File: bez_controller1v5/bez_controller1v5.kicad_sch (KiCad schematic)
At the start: 87 parts, among them J1 Conn_01x03_Male, J10 Conn_01x07_Socket, J11 Conn_01x03_Male, J12 Conn_01x03_Male, J13 USB_B_Mini, J14 JTAG Conn_01x06_Male, J16 MOLEX_Conn_Button, J17 MOLEX_Conn_Button, J2 Conn_01x03_Male, J3 Conn_01x03_Male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

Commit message: First iteration of the new board with new functions
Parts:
- removed J14: JTAG Conn_01x06_Male, Connector_PinHeader_2.54mm:PinHeader_1x06_P2.54mm_Vertical, symbol Connector:Conn_01x06_Male
- added J14: PPTC041LGBN-RC, KiCad:CONN_PPTC041LGBN-RC_SUL, symbol 2024-11-01_01-45-54:PPTC041LGBN-RC
- added J15: Conn_01x03_Male, Connector_PinHeader_2.54mm:PinHeader_1x03_P2.54mm_Vertical, symbol Connector:Conn_01x03_Male
- C10: footprint Capacitor_THT:CP_Radial_D5.0mm_P2.00mm -> Capacitor_SMD:C_0603_1608Metric
- J11, J12, J2, J3, J6, J7: footprint Connector_Molex:Molex_SPOX_5267-03A_1x03_P2.50mm_Vertical -> KiCad:CONN_S3B-XH-ALFSN_JST
- J13: footprint USB-Library:USB_MINI -> KiCad:USB_MINI
- J16, J17: footprint 530480210:MOLEX_530480210 -> KiCad:CON_530480210_MOL
- R17, R9: footprint (none) -> Resistor_SMD:R_0603_1608Metric
- U11, U12, U2, U3, U8, U9: footprint Package_SO:VSSOP-8_3.0x3.0mm_P0.65mm -> KiCad:VSSOP-8_3.0x3.0mm_P0.65mm
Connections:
- net +12V: no longer C11.2, C12.2, C21.2, C22.2, C24.2, C25.2, J11.2 (Pin_2), J12.2 (Pin_2), J2.2 (Pin_2), J3.2 (Pin_2), J6.2 (Pin_2), J7.2 (Pin_2)
- net +3.3V: now also J14.2
- net GND: now also J14.1
- net INT1: now also U7.8 (PC0); no longer U7.51 (PC10)
- net INT2: now also U7.9 (PC1); no longer U7.52 (PC11)
- net SWO: now also J15.1 (Pin_1); no longer U7.55 (PB3)
- net USART3_TX: now also U7.51 (PC10); no longer U7.29 (PB10)
- net post_shunt_12v: now reaches C2.1, R3.2, U1.1 (VI), U6.4 (-)
- net post_shunt_12v: now also C11.2, C12.2, C21.2, C22.2, C24.2, C25.2, J11.2 (Pin_2), J12.2 (Pin_2), J2.2 (Pin_2), J3.2 (Pin_2), J6.2 (Pin_2), J7.2 (Pin_2)
- net GPIO3: no longer names the net of U7.2 (PC13)
- new net SWO_or_Screen_SDA: J15.2 (Pin_2), U7.55 (PB3)
- new net Screen_SCL: J14.3, U7.29 (PB10)
- new net Screen_SDA: J14.4, J15.3 (Pin_3)
- no-connect marks 26 -> 24
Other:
- note added: "Adding Screen I2C Connection"
- note added: "Configure SWO or Screen"

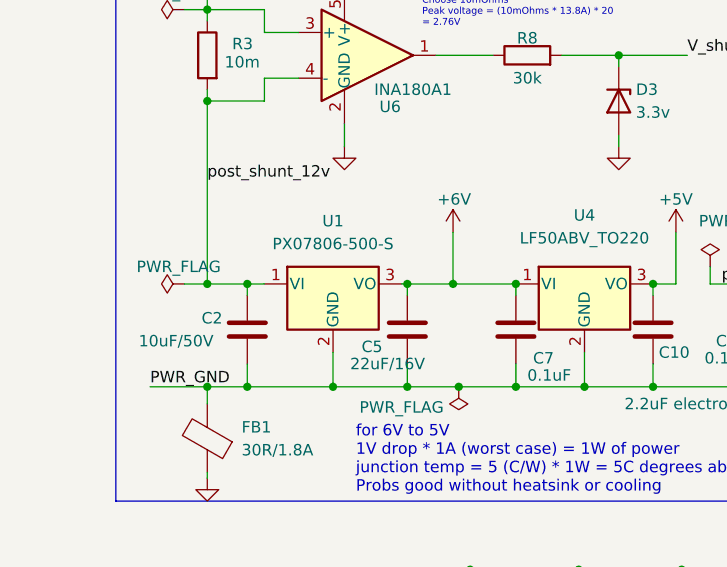
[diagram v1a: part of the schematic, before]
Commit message: -added label on each motor connections, -thickened 3.3v wires, removed uart line squiggles, updated U1 12v to 6v dcdc converter to new pxo7806-500
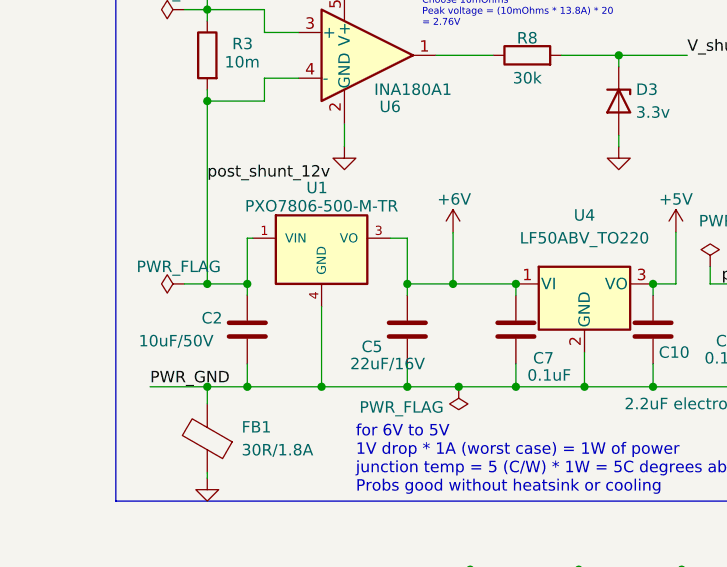
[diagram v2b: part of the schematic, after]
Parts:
- removed U1: PX07806-500-S, Package_TO_SOT_THT:TO-220F-3_Vertical, symbol Regulator_Linear:LM7805_TO220
- added U1: ~, KiCad:CONV_PXO7806-500-M-TR, symbol Regulator_Linear:PXO7806-500-M-TR
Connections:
- net +6V: now also U1.3 (VO)
- net PWR_GND: now also U1.4 (GND)
- net post_shunt_12v: now also U1.1 (VIN)
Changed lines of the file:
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@@
 	)
 	(junction
-		(at 36.83 68.58)
-		(diameter 0)
-		(color 0 0 0 0)
-	)
-	(junction
 		(at 43.18 182.88)
 		(diameter 0)
@@
 	)
 	(junction
+		(at 35.56 68.58)
+		(diameter 0)
+		(color 0 0 0 0)
+	)
+	(junction
 		(at 69.85 -52.07)
 		(diameter 0)
@@
 	(wire
 		(pts
+			(xy 35.56 68.58) (xy 45.085 68.58)
+		)
+		(stroke
+			(width 0)
+			(type default)
+		)
+	)
+	(wire
+		(pts
 			(xy 234.95 -102.235) (xy 267.97 -102.235)
 		)
@@
 	(wire
 		(pts
+			(xy 27.305 52.07) (xy 27.305 57.15)
+		)
+		(stroke
+			(width 0)
+			(type default)
+		)
+	)
+	(wire
+		(pts
 			(xy 121.92 96.52) (xy 121.92 99.06)
 		)
@@
 	(wire
 		(pts
-			(xy 27.305 57.15) (xy 29.21 57.15)
+			(xy 27.305 52.07) (xy 27.94 52.07)
 		)
 		(stroke
@@
 	(wire
 		(pts
-			(xy 44.45 57.15) (xy 45.085 57.15)
+			(xy 43.18 52.07) (xy 45.085 52.07)
 		)
 		(stroke
@@
 	(wire
 		(pts
+			(xy 45.085 52.07) (xy 45.085 57.15)
+		)
+		(stroke
+			(width 0)
+			(type default)
+		)
+	)
+	(wire
+		(pts
 			(xy 274.32 -102.235) (xy 274.32 -101.6)
 		)
@@
 	(wire
 		(pts
-			(xy 36.83 64.77) (xy 36.83 68.58)
+			(xy 35.56 59.69) (xy 35.56 68.58)
 		)
 		(stroke
@@
 	(wire
 		(pts
-			(xy 27.305 68.58) (xy 36.83 68.58)
+			(xy 27.305 68.58) (xy 35.56 68.58)
 		)
 		(stroke
@@
 	(wire
 		(pts
-			(xy 36.83 68.58) (xy 45.085 68.58)
-		)
-		(stroke
-			(width 0)
-			(type default)
-		)
-	)
-	(wire
-		(pts
 			(xy 138.43 53.34) (xy 145.415 53.34)
 		)
@@
 	)
 	(symbol
-		(lib_id "Regulator_Linear:LM7805_TO220")
-		(at 36.83 57.15 0)
-		(unit 1)
-		(exclude_from_sim no)
-		(in_bom yes)
-		(on_board yes)
-		(dnp no)
-		(fields_autoplaced yes)
-		(property "Reference" "U1"
-			(at 36.83 50.165 0)
-			(effects
-				(font
-					(size 1.27 1.27)
-				)
-			)
-		)
-		(property "Value" "PX07806-500-S"
-			(at 36.83 52.705 0)
-			(effects
-				(font
-					(size 1.27 1.27)
-				)
-			)
-		)
-		(property "Footprint" "Package_TO_SOT_THT:TO-220F-3_Vertical"
-			(at 36.83 51.435 0)
-			(effects
-				(font
-					(size 1.27 1.27)
-					(italic yes)
-				)
-				(hide yes)
-			)
-		)
-		(property "Datasheet" ""
-			(at 36.83 58.42 0)
-			(effects
-				(font
-					(size 1.27 1.27)
-				)
-				(hide yes)
-			)
-		)
-		(property "Description" ""
-			(at 36.83 57.15 0)
-			(effects
-				(font
-					(size 1.27 1.27)
-				)
-				(hide yes)
-			)
-		)
-		(pin "1"
-		)
-		(pin "2"
-		)
-		(pin "3"
-		)
-		(instances
-			(project "bez_controller1v5"
-				(path "/f1f9e721-9072-4626-979b-e86715e2d8d4"
-					(reference "U1")
-					(unit 1)
-				)
-			)
-		)
-	)
-	(symbol
 		(lib_id "power:+5V")
 		(at 86.36 -111.76 0)
@@
 					(unit 1)
 				)
+			)
+		)
+	)
+	(symbol
+		(lib_id "Regulator_Linear:PXO7806-500-M-TR")
+		(at 35.56 54.61 0)
+		(unit 1)
+		(exclude_from_sim no)
+		(in_bom yes)
+		(on_board yes)
+		(dnp no)
+		(property "Reference" "U1"
+			(at 35.052 46.482 0)
+			(effects
+				(font
+					(size 1.27 1.27)
+				)
+			)
+		)
+		(property "Value" "~"
+			(at 32.004 64.008 0)
+			(effects
+				(font
+					(size 1.27 1.27)
+				)
+				(justify left bottom)
+				(hide yes)
+			)
+		)
+		(property "Footprint" "KiCad:CONV_PXO7806-500-M-TR"
+			(at 39.37 54.61 0)
+			(effects
+				(font
+					(size 1.27 1.27)
+				)
+				(justify left bottom)
+				(hide yes)
+			)
+		)
+		(property "Datasheet" ""
+			(at 39.37 54.61 0)
+			(effects
+				(font
+					(size 1.27 1.27)
+				)
+				(justify left bottom)
+				(hide yes)
+			)
+		)
+		(property "Description" ""
+			(at 39.37 54.61 0)
+			(effects
+				(font
+					(size 1.27 1.27)
+				)
+				(hide yes)
+			)
+		)
+		(property "PARTREV" ""
+			(at 39.37 54.61 0)
+			(effects
+				(font
+					(size 1.27 1.27)
+				)
+				(justify left bottom)
+				(hide yes)
+			)
+		)
+		(property "SNAPEDA_PN" "PXO7806-500-M-TR"
+			(at 35.56 48.514 0)
+			(effects
+				(font
+					(size 1.27 1.27)
+				)
+			)
+		)
+		(property "MANUFACTURER" ""
+			(at 39.37 54.61 0)
+			(effects
+				(font
+					(size 1.27 1.27)
+				)
+				(justify left bottom)
+				(hide yes)
+			)
+		)
+		(property "MAXIMUM_PACKAGE_HEIGHT" ""
+			(at 33.274 46.482 0)
+			(effects
+				(font
+					(size 1.27 1.27)
+				)
+				(justify left bottom)
+				(hide yes)
+			)
+		)
+		(property "STANDARD" ""
+			(at 39.37 54.61 0)
+			(effects
+				(font
+					(size 1.27 1.27)
+				)
+				(justify left bottom)
+				(hide yes)
+			)
+		)
+		(pin "1"
+		)
+		(pin "3"
+		)
+		(pin "4"
+		)
+		(instances
+			(project ""
+				(path "/f1f9e721-9072-4626-979b-e86715e2d8d4"
+					(reference "U1")
+					(unit 1)
+				)

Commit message: Verified circuit; also added button as per Nam's request
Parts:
- J1: footprint Connector_PinHeader_2.54mm:PinHeader_1x03_P2.54mm_Vertical -> KiCad:BootloaderButton
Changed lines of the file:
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@@
 			)
 		)
-		(property "Footprint" "Connector_PinHeader_2.54mm:PinHeader_1x03_P2.54mm_Vertical"
+		(property "Footprint" "KiCad:BootloaderButton"
 			(at 76.2 116.84 0)
 			(effects

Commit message: Smaller board, changed header back to male, optimized some stuff
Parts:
- J4: footprint Connector_AMASS:AMASS_XT60PW-F_1x02_P7.20mm_Horizontal -> Connector_AMASS:AMASS_XT60PW-M_1x02_P7.20mm_Horizontal
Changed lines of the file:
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@@
 			)
 		)
-		(property "Footprint" "Connector_AMASS:AMASS_XT60PW-F_1x02_P7.20mm_Horizontal"
+		(property "Footprint" "Connector_AMASS:AMASS_XT60PW-M_1x02_P7.20mm_Horizontal"
 			(at 133.35 73.66 0)
 			(effects

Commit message: increased motor protection diode to 6.2 V
removed boot loader button

added a 5pin jst connection using same i2c connection as screen Please enter the commit message for your changes. Lines starting
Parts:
- removed J1: Conn_01x03_Male, KiCad:BootloaderButton, symbol Connector:Conn_01x03_Male
- added J1: B5B-PH-K-S, Connector_JST:JST_PH_B5B-PH-K_1x05_P2.00mm_Vertical, symbol Connector_Generic:Conn_01x05
- D10, D5, D6, D7, D8, D9: value BZV55B5V1 -> BZV55B6V2
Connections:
- net +3.3V: now also J1.2 (Pin_2)
- net GND: now also R6.1, J1.1 (Pin_1)
- net Screen_SCL: now also J1.3 (Pin_3)
- net Screen_SDA: now also J1.4 (Pin_4)
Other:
- note added: "Adding JST I2C Connection"
- moved on the sheet: C9

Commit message: Made some fixes
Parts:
- added J18: B5B-PH-K-S, Connector_JST:JST_PH_B5B-PH-K_1x05_P2.00mm_Vertical, symbol Connector_Generic:Conn_01x05
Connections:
- net +3.3V: no longer J1.2 (Pin_2)
- net GND: now also J18.1 (Pin_1)
- net Screen_SCL: now also J18.3 (Pin_3)
- net Screen_SDA: now also J18.4 (Pin_4)
- net power: now also J1.2 (Pin_2), J18.2 (Pin_2)
- net FootGPIO1: now reaches J1.5 (Pin_5)
- net FootGPIO1: now also U7.61 (PB8)
- net FootGPIO2: now reaches U7.57 (PB5)
- net FootGPIO2: now also J18.5 (Pin_5)
- no-connect marks 24 -> 22
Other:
- moved on the sheet: J1, U1

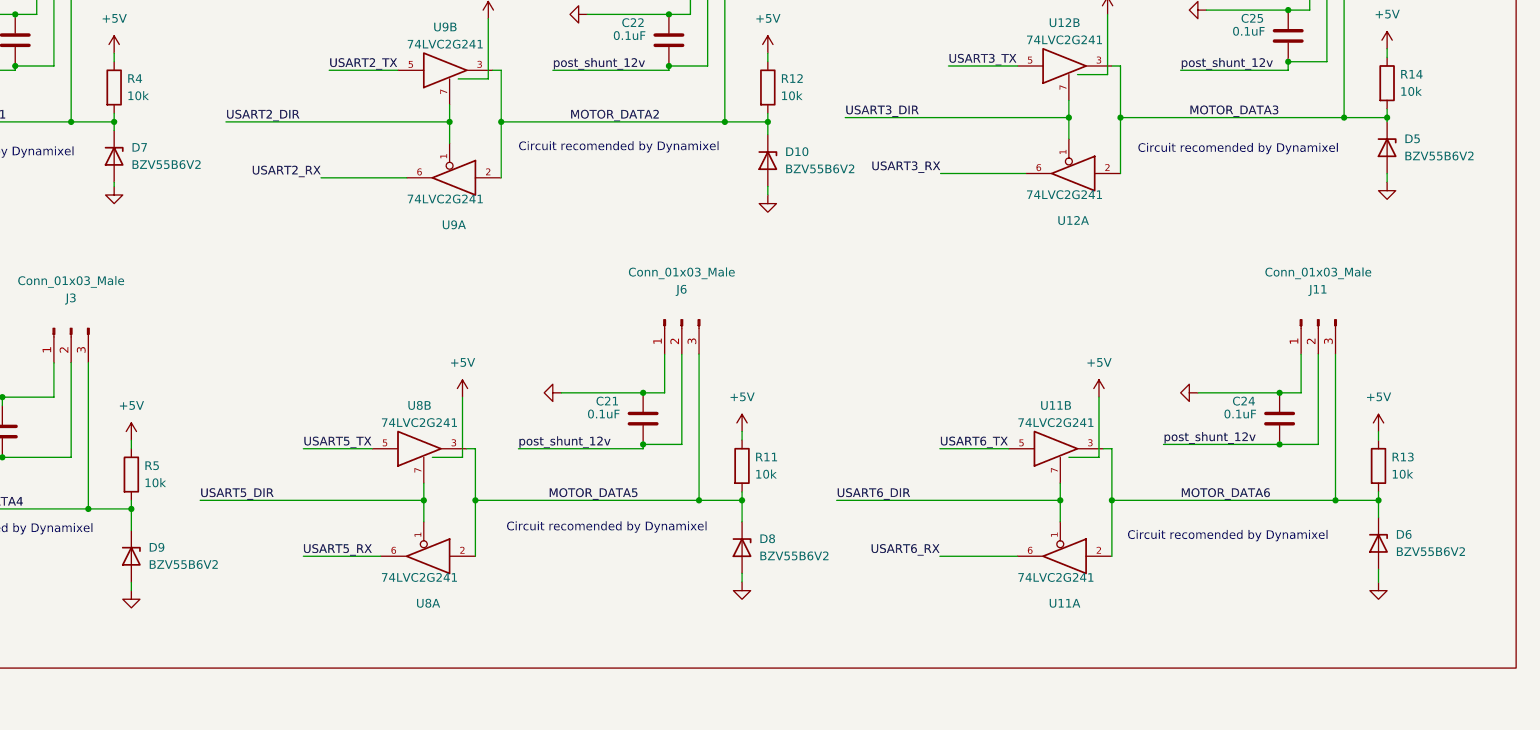
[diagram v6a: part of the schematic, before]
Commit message: updated motor protection tvs diode and kelvin sense circuit to sensing
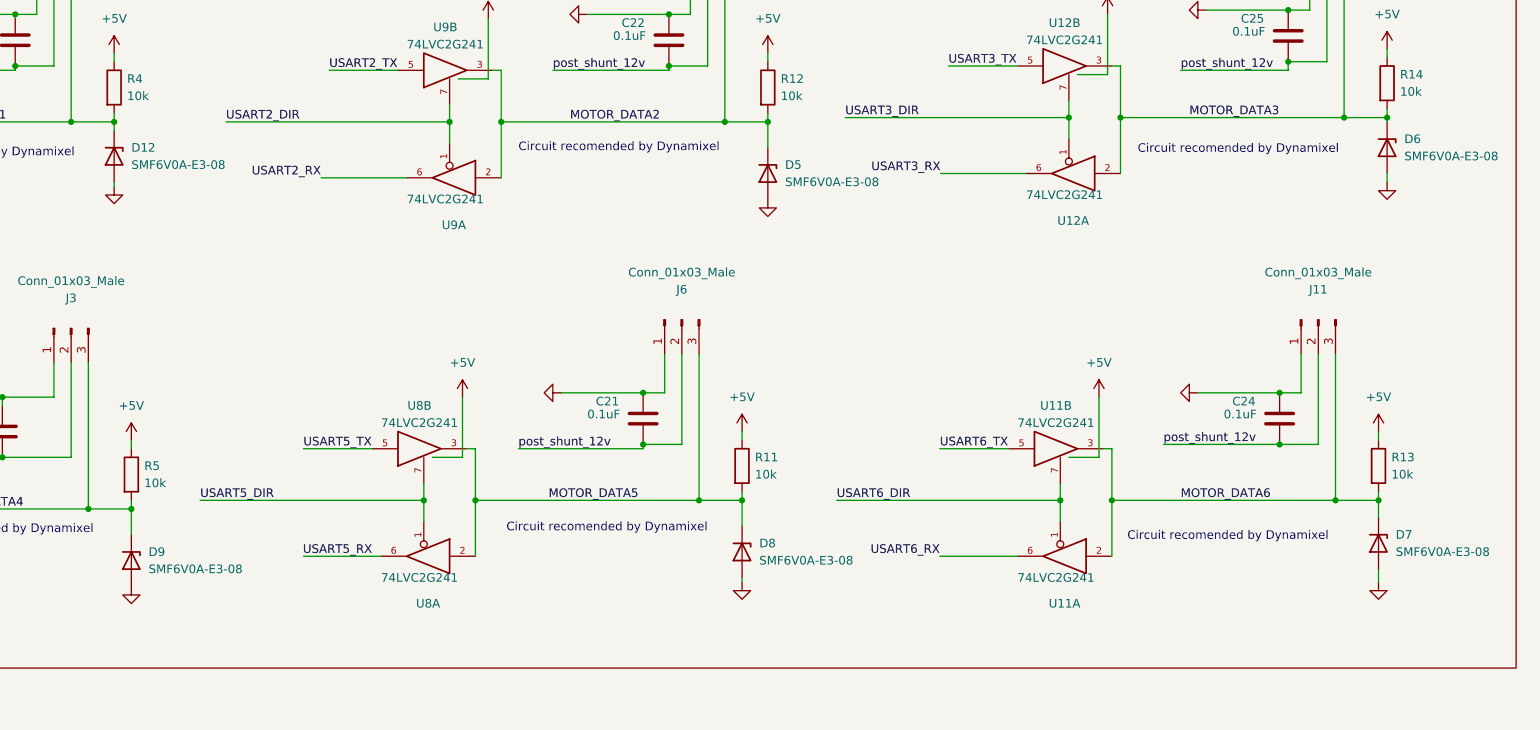
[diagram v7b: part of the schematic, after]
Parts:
- removed D10, D5, D6, D7, D8, D9: BZV55B6V2, Diode_SMD:D_MiniMELF, symbol Diode:BZV55B5V1
- added D12, D5, D6, D7, D8, D9: SMF6V0A-E3-08, KiCad:D_SMF, symbol Device:D_Zener
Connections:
- net GND: now also D12.2 (A), D5.2 (A), D6.2 (A), D7.2 (A), D8.2 (A), D9.2 (A)
- net MOTOR_DATA1: now also D12.1 (K)
- net MOTOR_DATA2: now also D5.1 (K)
- net MOTOR_DATA3: now also D6.1 (K)
- net MOTOR_DATA4: now also D9.1 (K)
- net MOTOR_DATA5: now also D8.1 (K)
- net MOTOR_DATA6: now also D7.1 (K)

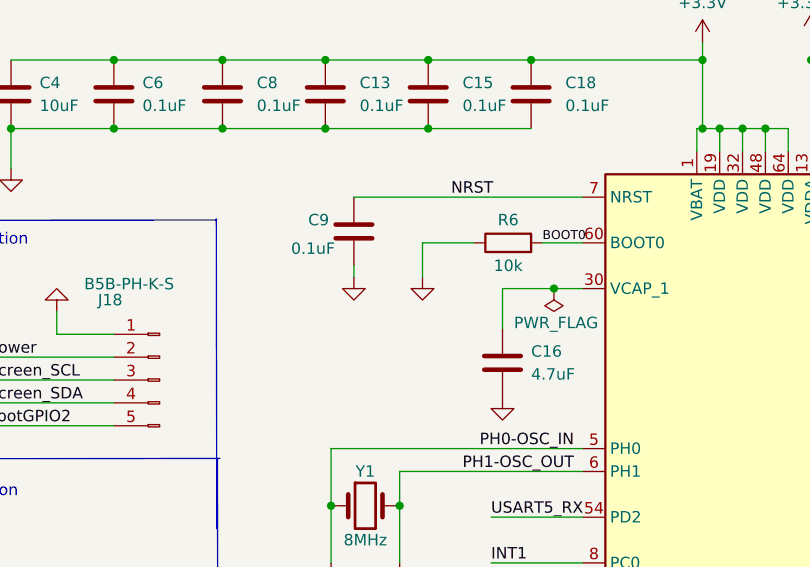
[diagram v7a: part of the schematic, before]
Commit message: re-added the bootloader button
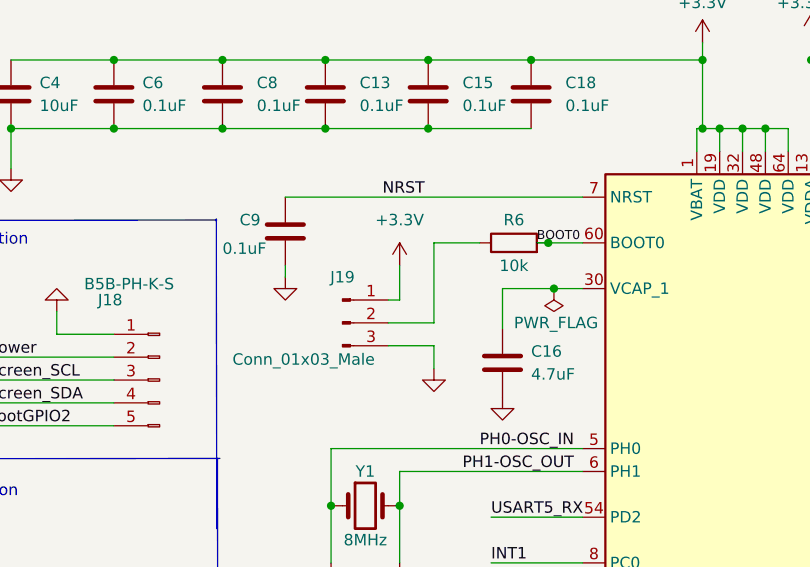
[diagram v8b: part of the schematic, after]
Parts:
- added J19: Conn_01x03_Male, KiCad:BootloaderButton, symbol Connector:Conn_01x03_Pin
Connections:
- net +3.3V: now also J19.1 (Pin_1)
- net GND: now also J19.3 (Pin_3); no longer R6.1
- new net: J19.2 (Pin_2), R6.1
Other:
- moved on the sheet: C9, R6
